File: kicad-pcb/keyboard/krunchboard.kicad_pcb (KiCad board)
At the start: 2 copper layers, 427.6 x 139.1 mm, 212 parts, among them J1 Conn_01x04_Pin, J2 Conn_01x04_Pin, SW1 SW_Push_45deg, SW10 SW_Push_45deg, SW11 SW_Push_45deg, SW12 SW_Push_45deg, SW13 SW_Push_45deg, SW14 SW_Push_45deg, SW15 SW_Push_45deg, SW16 SW_Push_45deg, SW17 SW_Push_45deg, SW18 SW_Push_45deg, SW19 SW_Push_45deg, SW2 SW_Push_45deg, SW20 SW_Push_45deg, SW21 SW_Push_45deg, SW22 SW_Push_45deg, SW23 SW_Push_45deg, SW24 SW_Push_45deg, SW25 SW_Push_45deg, SW26 SW_Push_45deg, SW27 SW_Push_45deg, SW28 SW_Push_45deg, SW29 SW_Push_45deg, SW3 SW_Push_45deg, SW30 SW_Push_45deg, SW31 SW_Push_45deg, SW32 SW_Push_45deg, SW33 SW_Push_45deg, SW34 SW_Push_45deg, SW35 SW_Push_45deg, SW36 SW_Push_45deg, SW37 SW_Push_45deg, SW38 SW_Push_45deg, SW39 SW_Push_45deg, SW4 SW_Push_45deg, SW40 SW_Push_45deg, SW41 SW_Push_45deg, SW42 SW_Push_45deg, SW43 SW_Push_45deg, SW44 SW_Push_45deg, SW45 SW_Push_45deg, SW46 SW_Push_45deg, SW47 SW_Push_45deg, SW48 SW_Push_45deg, SW49 SW_Push_45deg, SW5 SW_Push_45deg, SW50 SW_Push_45deg, SW51 SW_Push_45deg, SW52 SW_Push_45deg, SW53 SW_Push_45deg, SW54 SW_Push_45deg, SW55 SW_Push_45deg, SW56 SW_Push_45deg, SW57 SW_Push_45deg, SW58 SW_Push_45deg, SW59 SW_Push_45deg, SW6 SW_Push_45deg, SW60 SW_Push_45deg, SW61 SW_Push_45deg, SW62 SW_Push_45deg, SW63 SW_Push_45deg, SW64 SW_Push_45deg, SW65 SW_Push_45deg, SW66 SW_Push_45deg, SW67 SW_Push_45deg, SW68 SW_Push_45deg, SW69 SW_Push_45deg, SW7 SW_Push_45deg, SW70 SW_Push_45deg, SW71 SW_Push_45deg, SW72 SW_Push_45deg, SW73 SW_Push_45deg, SW74 SW_Push_45deg, SW75 SW_Push_45deg, SW76 SW_Push_45deg, SW77 SW_Push_45deg, SW78 SW_Push_45deg, SW79 SW_Push_45deg, SW8 SW_Push_45deg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

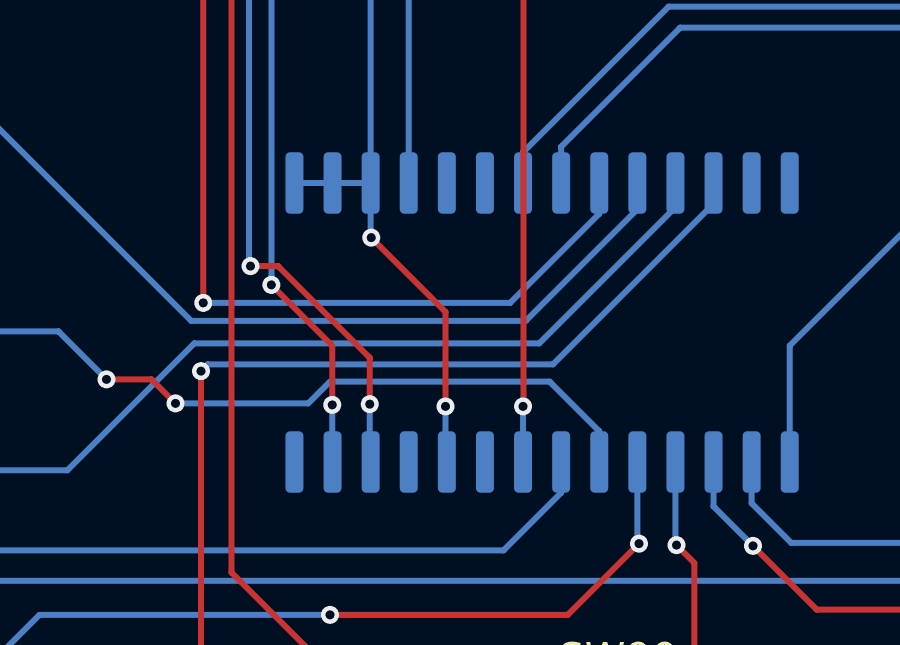
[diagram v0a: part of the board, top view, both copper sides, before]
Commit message: switched mounting styles, updated pcb, plate, and case
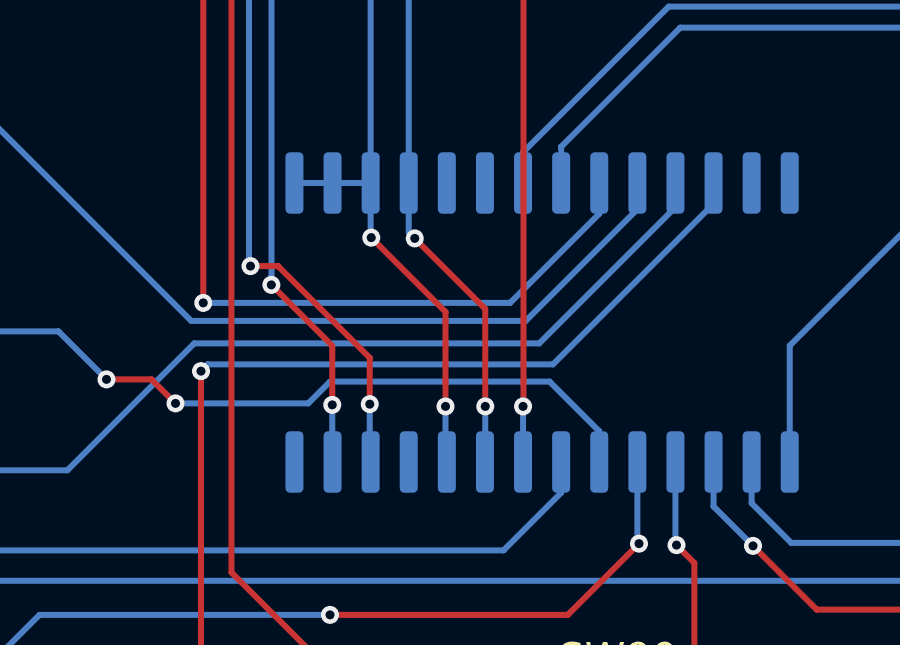
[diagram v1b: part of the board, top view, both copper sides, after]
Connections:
- U1 pad 9: unconnected-(U1-VDD-Pad9) -> +3V3
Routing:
- net +3V3: track 291.5 -> 301.8 mm, vias 7 -> 9
